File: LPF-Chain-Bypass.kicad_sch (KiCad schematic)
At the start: 2 parts, among them K9 HK19F-DCxxV-SHC, SW2 SW_SPDT

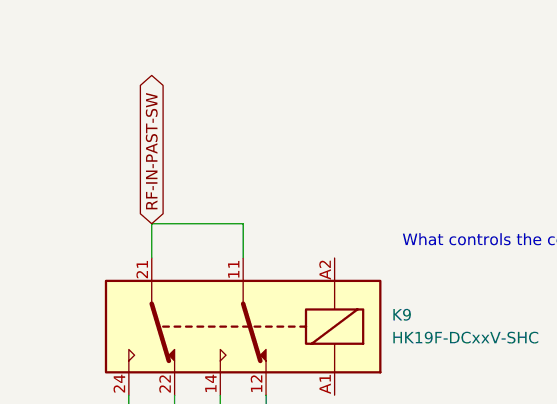
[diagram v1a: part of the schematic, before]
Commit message: RF-IN-PAST-SW now RF-INTO-FILTERS
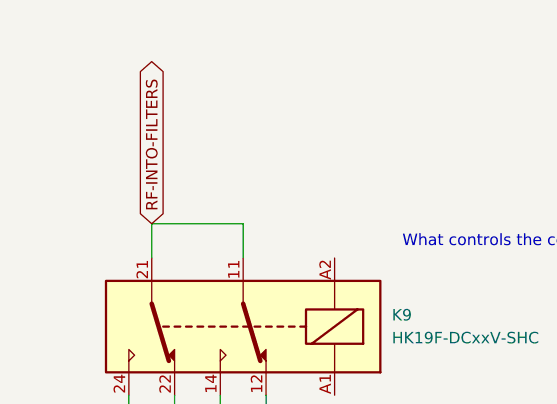
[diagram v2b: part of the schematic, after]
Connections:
- net RF-IN-PAST-SW renamed RF-INTO-FILTERS
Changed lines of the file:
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@@
 		)
 	)
-	(global_label "RF-IN-PAST-SW"
+	(global_label "RF-INTO-FILTERS"
 		(shape bidirectional)
 		(at 57.15 78.74 90)
@@
 		)
 		(property "Intersheetrefs" "${INTERSHEET_REFS}"
-			(at 57.15 58.436 90)
+			(at 57.15 57.5893 90)
 			(effects
 				(font

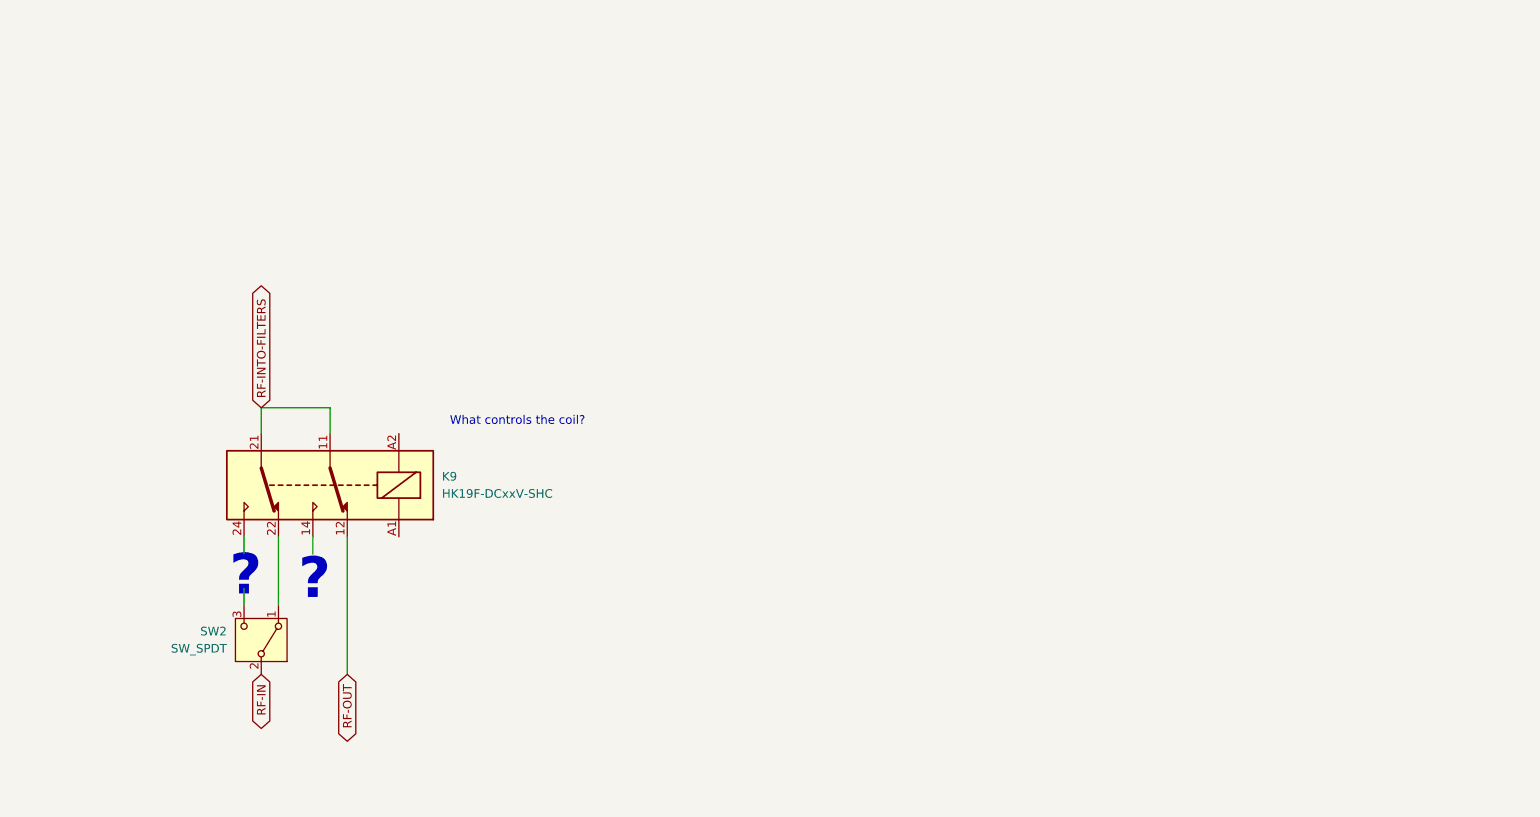
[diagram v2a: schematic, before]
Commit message: trying to get K1 & K2 appear in multiple places, yet be recognized as identical.  Currently reporting dup K1
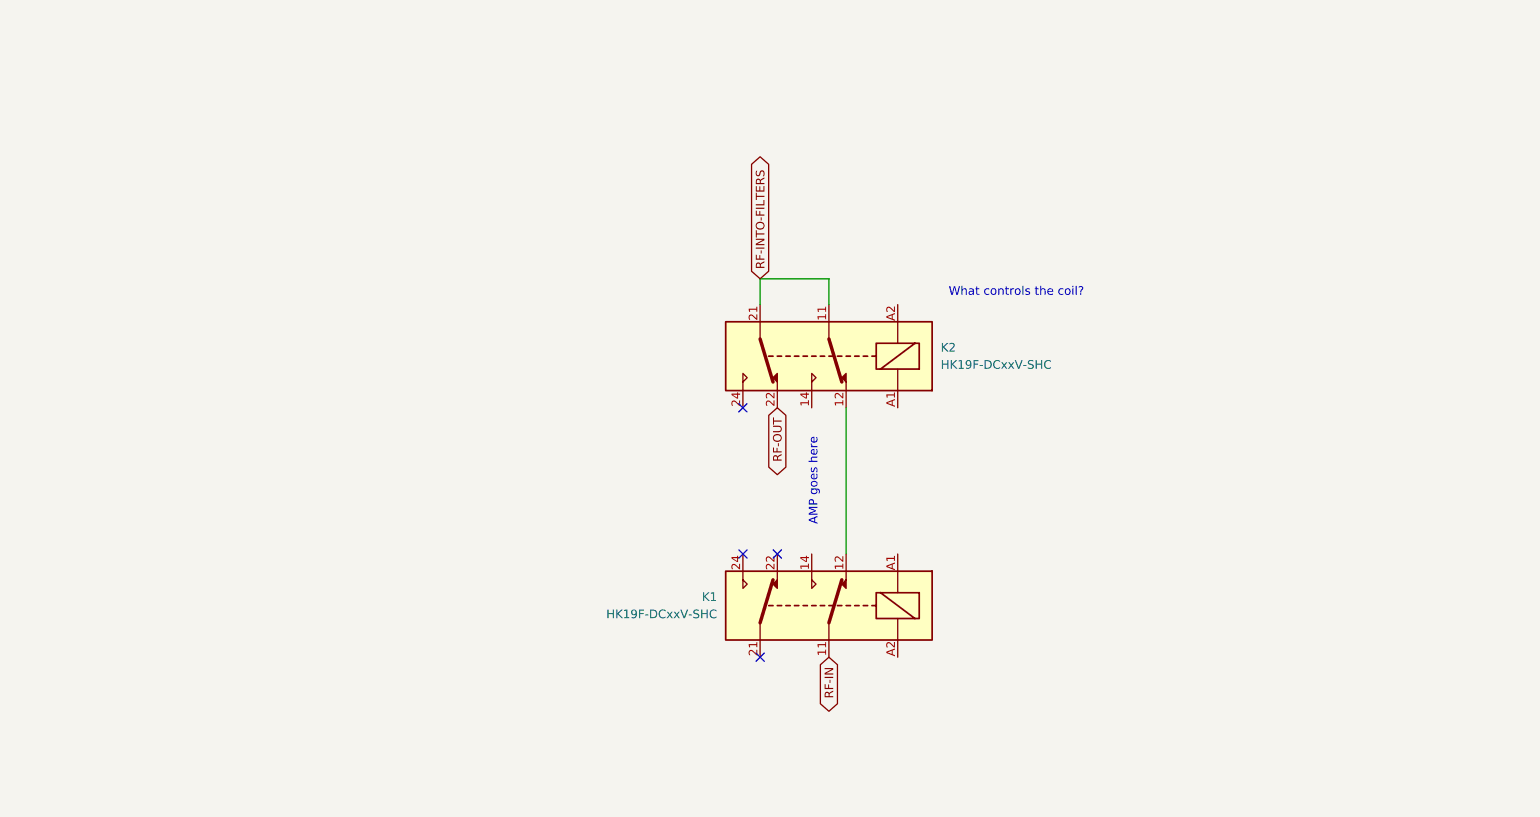
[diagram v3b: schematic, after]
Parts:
- removed SW2: SW_SPDT, symbol Switch:SW_SPDT
- added K1: HK19F-DCxxV-SHC, Relay_THT:Relay_DPDT_Finder_30.22, symbol Relay:HK19F-DCxxV-SHC
- renumbered K9 to K2
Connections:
- net RF-IN: now also K1.11
- net RF-OUT: now also K2.22; no longer K2.12
- new net: K1.12, K2.12
- no-connect marks 0 -> 4
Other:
- note added: "AMP goes here"
- note removed: "?"
- moved on the sheet: K2
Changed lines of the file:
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@@
 		(company "WA7GIL")
 	)
-	(wire
-		(pts
-			(xy 57.15 78.74) (xy 67.31 78.74)
-		)
-		(stroke
-			(width 0)
-			(type default)
-		)
-	)
-	(wire
-		(pts
-			(xy 69.85 97.79) (xy 69.85 118.11)
-		)
-		(stroke
-			(width 0)
-			(type default)
-		)
-	)
-	(wire
-		(pts
-			(xy 57.15 82.55) (xy 57.15 78.74)
-		)
-		(stroke
-			(width 0)
-			(type default)
-		)
-	)
-	(wire
-		(pts
-			(xy 64.77 97.79) (xy 64.77 100.33)
-		)
-		(stroke
-			(width 0)
-			(type default)
-		)
-	)
-	(wire
-		(pts
-			(xy 59.69 97.79) (xy 59.69 107.95)
-		)
-		(stroke
-			(width 0)
-			(type default)
-		)
-	)
-	(wire
-		(pts
-			(xy 54.61 100.33) (xy 54.61 97.79)
-		)
-		(stroke
-			(width 0)
-			(type default)
-		)
-	)
-	(wire
-		(pts
-			(xy 67.31 78.74) (xy 67.31 82.55)
-		)
-		(stroke
-			(width 0)
-			(type default)
-		)
-	)
-	(wire
-		(pts
-			(xy 54.61 105.41) (xy 54.61 107.95)
-		)
-		(stroke
-			(width 0)
-			(type default)
-		)
-	)
-	(text "?"
-		(exclude_from_sim no)
-		(at 54.864 103.632 0)
-		(effects
-			(font
-				(size 6 6)
-				(thickness 1.2)
-				(bold yes)
-			)
-		)
-	)
-	(text "?"
-		(exclude_from_sim no)
-		(at 65.024 104.14 0)
-		(effects
-			(font
-				(size 6 6)
-				(thickness 1.2)
-				(bold yes)
+	(no_connect
+		(at 128.27 100.33)
+	)
+	(no_connect
+		(at 130.81 115.57)
+	)
+	(no_connect
+		(at 133.35 100.33)
+	)
+	(no_connect
+		(at 128.27 78.74)
+	)
+	(wire
+		(pts
+			(xy 130.81 59.69) (xy 140.97 59.69)
+		)
+		(stroke
+			(width 0)
+			(type default)
+		)
+	)
+	(wire
+		(pts
+			(xy 143.51 78.74) (xy 143.51 100.33)
+		)
+		(stroke
+			(width 0)
+			(type default)
+		)
+	)
+	(wire
+		(pts
+			(xy 130.81 63.5) (xy 130.81 59.69)
+		)
+		(stroke
+			(width 0)
+			(type default)
+		)
+	)
+	(wire
+		(pts
+			(xy 140.97 59.69) (xy 140.97 63.5)
+		)
+		(stroke
+			(width 0)
+			(type default)
+		)
+	)
+	(text "AMP goes here"
+		(exclude_from_sim no)
+		(at 138.684 89.662 90)
+		(effects
+			(font
+				(size 1.27 1.27)
 			)
 		)
@@
 	(text "What controls the coil?"
 		(exclude_from_sim no)
-		(at 94.996 80.772 0)
+		(at 168.656 61.722 0)
 		(effects
 			(font
@@
 	(global_label "RF-OUT"
 		(shape bidirectional)
-		(at 69.85 118.11 270)
+		(at 133.35 78.74 270)
 		(fields_autoplaced yes)
 		(effects
@@
 		)
 		(property "Intersheetrefs" "${INTERSHEET_REFS}"
-			(at 69.85 129.7659 90)
+			(at 133.35 90.3959 90)
 			(effects
 				(font
@@
 	(global_label "RF-INTO-FILTERS"
 		(shape bidirectional)
-		(at 57.15 78.74 90)
+		(at 130.81 59.69 90)
 		(fields_autoplaced yes)
 		(effects
@@
 		)
 		(property "Intersheetrefs" "${INTERSHEET_REFS}"
-			(at 57.15 57.5893 90)
+			(at 130.81 38.5393 90)
 			(effects
 				(font
@@
 	(global_label "RF-IN"
 		(shape bidirectional)
-		(at 57.15 118.11 270)
+		(at 140.97 115.57 270)
 		(fields_autoplaced yes)
 		(effects
@@
 		)
 		(property "Intersheetrefs" "${INTERSHEET_REFS}"
-			(at 57.15 128.0726 90)
+			(at 140.97 125.5326 90)
 			(effects
 				(font
@@
 	)
 	(symbol
-		(lib_id "Switch:SW_SPDT")
-		(at 57.15 113.03 270)
-		(mirror x)
+		(lib_id "Relay:HK19F-DCxxV-SHC")
+		(at 140.97 71.12 180)
 		(unit 1)
 		(exclude_from_sim no)
@@
 		(on_board yes)
 		(dnp no)
-		(property "Reference" "SW2"
-			(at 52.07 111.7599 90)
-			(effects
-				(font
-					(size 1.27 1.27)
-				)
-				(justify right)
-			)
-		)
-		(property "Value" "SW_SPDT"
-			(at 52.07 114.2999 90)
-			(effects
-				(font
-					(size 1.27 1.27)
-				)
-				(justify right)
-			)
-		)
-		(property "Footprint" ""
-			(at 57.15 113.03 0)
-			(effects
-				(font
-					(size 1.27 1.27)
-				)
-				(hide yes)
-			)
-		)
-		(property "Datasheet" "~"
-			(at 49.53 113.03 0)
-			(effects
-				(font
-					(size 1.27 1.27)
-				)
-				(hide yes)
-			)
-		)
-		(property "Description" "Switch, single pole double throw"
-			(at 57.15 113.03 0)
-			(effects
-				(font
-					(size 1.27 1.27)
-				)
-				(hide yes)
-			)
-		)
-		(pin "3"
-		)
-		(pin "1"
-		)
-		(pin "2"
+		(fields_autoplaced yes)
+		(property "Reference" "K2"
+			(at 157.48 69.8499 0)
+			(effects
+				(font
+					(size 1.27 1.27)
+				)
+				(justify right)
+			)
+		)
+		(property "Value" "HK19F-DCxxV-SHC"
+			(at 157.48 72.3899 0)
+			(effects
+				(font
+					(size 1.27 1.27)
+				)
+				(justify right)
+			)
+		)
+		(property "Footprint" "Relay_THT:Relay_DPDT_Finder_30.22"
+			(at 158.75 58.42 0)
+			(effects
+				(font
+					(size 1.27 1.27)
+				)
+				(justify left)
+				(hide yes)
+			)
+		)
+		(property "Datasheet" "https://www.lcsc.com/datasheet/lcsc_datasheet_1810201512_Ningbo-Keke-New-Era-Appliance-HK19F-DC12V-SHG_C42803.pdf"
+			(at 140.97 53.34 0)
+			(effects
+				(font
+					(size 1.27 1.27)
+				)
+				(hide yes)
+			)
+		)
+		(property "Description" "HuiKe 19F monostable relay, DPDT, 1A"
+			(at 139.7 55.88 0)
+			(effects
+				(font
+					(size 1.27 1.27)
+				)
+				(hide yes)
+			)
+		)
+		(pin "11"
+		)
+		(pin "14"
+		)
+		(pin "21"
+		)
+		(pin "12"
+		)
+		(pin "22"
+		)
+		(pin "A2"
+		)
+		(pin "A1"
+		)
+		(pin "24"
 		)
 		(instances
 			(project ""
 				(path "/e63e39d7-6ac0-4ffd-8aa3-1841a4541b55/437da5b9-3c1b-43a3-b733-5d9a574d228b"
-					(reference "SW2")
+					(reference "K2")
 					(unit 1)
 				)
@@
 	(symbol
 		(lib_id "Relay:HK19F-DCxxV-SHC")
-		(at 67.31 90.17 180)
+		(at 140.97 107.95 0)
+		(mirror y)
 		(unit 1)
 		(exclude_from_sim no)
@@
 		(on_board yes)
 		(dnp no)
-		(fields_autoplaced yes)
-		(property "Reference" "K9"
-			(at 83.82 88.8999 0)
-			(effects
-				(font
-					(size 1.27 1.27)
-				)
-				(justify right)
+		(property "Reference" "K1"
+			(at 124.46 106.6799 0)
+			(effects
+				(font
+					(size 1.27 1.27)
+				)
+				(justify left)
 			)
 		)
 		(property "Value" "HK19F-DCxxV-SHC"
-			(at 83.82 91.4399 0)
-			(effects
-				(font
-					(size 1.27 1.27)
-				)
-				(justify right)
+			(at 124.46 109.2199 0)
+			(effects
+				(font
+					(size 1.27 1.27)
+				)
+				(justify left)
 			)
 		)
 		(property "Footprint" "Relay_THT:Relay_DPDT_Finder_30.22"
-			(at 85.09 77.47 0)
+			(at 158.75 120.65 0)
 			(effects
 				(font
@@
 		)
 		(property "Datasheet" "https://www.lcsc.com/datasheet/lcsc_datasheet_1810201512_Ningbo-Keke-New-Era-Appliance-HK19F-DC12V-SHG_C42803.pdf"
-			(at 67.31 72.39 0)
+			(at 140.97 125.73 0)
 			(effects
 				(font
@@
 		)
 		(property "Description" "HuiKe 19F monostable relay, DPDT, 1A"
-			(at 66.04 74.93 0)
-			(effects
-				(font
-					(size 1.27 1.27)
-				)
-				(hide yes)
-			)
+			(at 139.7 123.19 0)
+			(effects
+				(font
+					(size 1.27 1.27)
+				)
+				(hide yes)
+			)
+		)
+		(pin "A2"
+		)
+		(pin "A1"
+		)
+		(pin "22"
+		)
+		(pin "21"
+		)
+		(pin "24"
+		)
+		(pin "14"
+		)
+		(pin "12"
 		)
 		(pin "11"
 		)
-		(pin "14"
-		)
-		(pin "21"
-		)
-		(pin "12"
-		)
-		(pin "22"
-		)
-		(pin "A2"
-		)
-		(pin "A1"
-		)
-		(pin "24"
-		)
 		(instances
-			(project ""
+			(project "QMX-amp"
 				(path "/e63e39d7-6ac0-4ffd-8aa3-1841a4541b55/437da5b9-3c1b-43a3-b733-5d9a574d228b"
-					(reference "K9")
+					(reference "K1")
 					(unit 1)
 				)

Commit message: checkpoint progress from 240810
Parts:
- added C99: C_Polarized, symbol Device:C_Polarized
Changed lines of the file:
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@@
+		)
+	)
+	(symbol
+		(lib_id "Device:C_Polarized")
+		(at 209.55 133.35 0)
+		(unit 1)
+		(exclude_from_sim no)
+		(in_bom yes)
+		(on_board yes)
+		(dnp no)
+		(fields_autoplaced yes)
+		(property "Reference" "C99"
+			(at 213.36 131.1909 0)
+			(effects
+				(font
+					(size 1.27 1.27)
+				)
+				(justify left)
+			)
+		)
+		(property "Value" "C_Polarized"
+			(at 213.36 133.7309 0)
+			(effects
+				(font
+					(size 1.27 1.27)
+				)
+				(justify left)
+			)
+		)
+		(property "Footprint" ""
+			(at 210.5152 137.16 0)
+			(effects
+				(font
+					(size 1.27 1.27)
+				)
+				(hide yes)
+			)
+		)
+		(property "Datasheet" "~"
+			(at 209.55 133.35 0)
+			(effects
+				(font
+					(size 1.27 1.27)
+				)
+				(hide yes)
+			)
+		)
+		(property "Description" "Polarized capacitor"
+			(at 209.55 133.35 0)
+			(effects
+				(font
+					(size 1.27 1.27)
+				)
+				(hide yes)
+			)
+		)
+		(pin "2"
+		)
+		(pin "1"
+		)
+		(instances
+			(project "QMX-amp"
+				(path "/e63e39d7-6ac0-4ffd-8aa3-1841a4541b55/437da5b9-3c1b-43a3-b733-5d9a574d228b"
+					(reference "C99")
+					(unit 1)
+				)
+			)
 		)
 	)

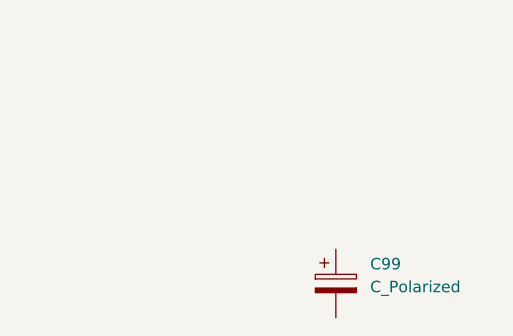
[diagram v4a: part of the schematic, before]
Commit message: changed +5V and +12V from global symbol to the more normal voltage busses
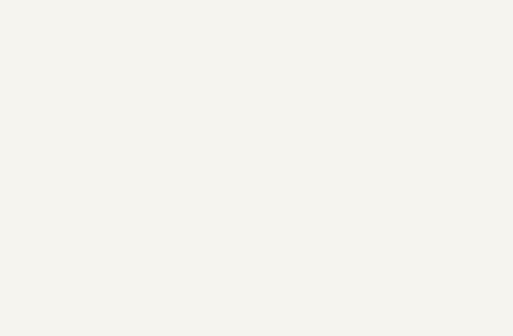
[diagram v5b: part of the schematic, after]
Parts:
- removed C99: C_Polarized, symbol Device:C_Polarized
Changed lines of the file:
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@@
-		)
-	)
-	(symbol
-		(lib_id "Device:C_Polarized")
-		(at 209.55 133.35 0)
-		(unit 1)
-		(exclude_from_sim no)
-		(in_bom yes)
-		(on_board yes)
-		(dnp no)
-		(fields_autoplaced yes)
-		(property "Reference" "C99"
-			(at 213.36 131.1909 0)
-			(effects
-				(font
-					(size 1.27 1.27)
-				)
-				(justify left)
-			)
-		)
-		(property "Value" "C_Polarized"
-			(at 213.36 133.7309 0)
-			(effects
-				(font
-					(size 1.27 1.27)
-				)
-				(justify left)
-			)
-		)
-		(property "Footprint" ""
-			(at 210.5152 137.16 0)
-			(effects
-				(font
-					(size 1.27 1.27)
-				)
-				(hide yes)
-			)
-		)
-		(property "Datasheet" "~"
-			(at 209.55 133.35 0)
-			(effects
-				(font
-					(size 1.27 1.27)
-				)
-				(hide yes)
-			)
-		)
-		(property "Description" "Polarized capacitor"
-			(at 209.55 133.35 0)
-			(effects
-				(font
-					(size 1.27 1.27)
-				)
-				(hide yes)
-			)
-		)
-		(pin "2"
-		)
-		(pin "1"
-		)
-		(instances
-			(project "QMX-amp"
-				(path "/e63e39d7-6ac0-4ffd-8aa3-1841a4541b55/437da5b9-3c1b-43a3-b733-5d9a574d228b"
-					(reference "C99")
-					(unit 1)
-				)
-			)
 		)
 	)

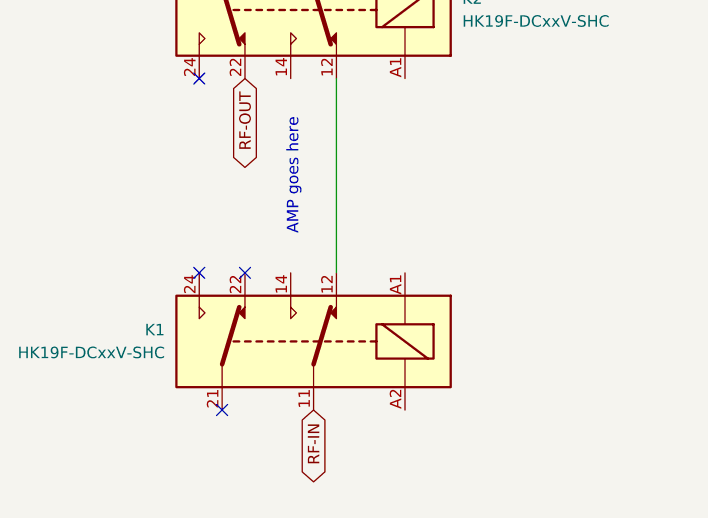
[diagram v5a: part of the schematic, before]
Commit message: could not figure out how to have two instances of K1 so I used global labels.  STINKY HACK
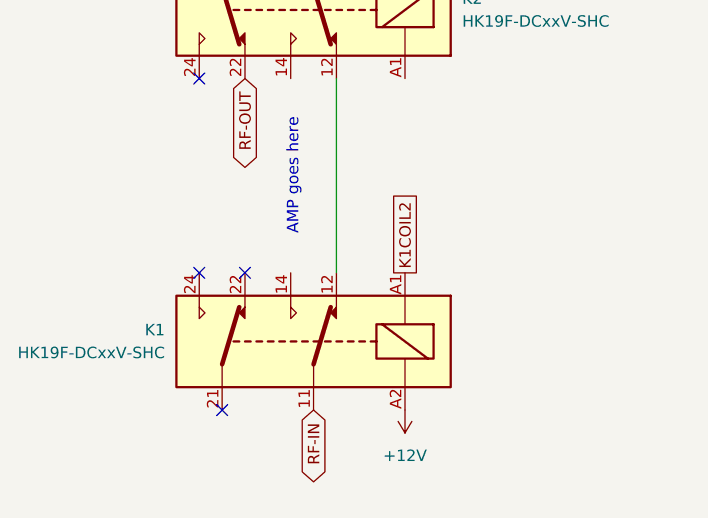
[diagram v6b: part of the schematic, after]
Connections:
- net K1COIL2: now reaches K1.A1
- net +12V: now reaches K1.A2
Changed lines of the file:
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@@
+		)
+	)
+	(global_label "K1COIL2"
+		(shape passive)
+		(at 151.13 100.33 90)
+		(fields_autoplaced yes)
+		(effects
+			(font
+				(size 1.27 1.27)
+			)
+			(justify left)
+		)
+		(property "Intersheetrefs" "${INTERSHEET_REFS}"
+			(at 151.13 90.3433 90)
+			(effects
+				(font
+					(size 1.27 1.27)
+				)
+				(justify left)
+				(hide yes)
+			)
+		)
+	)
+	(symbol
+		(lib_id "power:+12V")
+		(at 151.13 115.57 180)
+		(unit 1)
+		(exclude_from_sim no)
+		(in_bom yes)
+		(on_board yes)
+		(dnp no)
+		(fields_autoplaced yes)
+		(property "Reference" "#PWR033"
+			(at 151.13 111.76 0)
+			(effects
+				(font
+					(size 1.27 1.27)
+				)
+				(hide yes)
+			)
+		)
+		(property "Value" "+12V"
+			(at 151.13 120.65 0)
+			(effects
+				(font
+					(size 1.27 1.27)
+				)
+			)
+		)
+		(property "Footprint" ""
+			(at 151.13 115.57 0)
+			(effects
+				(font
+					(size 1.27 1.27)
+				)
+				(hide yes)
+			)
+		)
+		(property "Datasheet" ""
+			(at 151.13 115.57 0)
+			(effects
+				(font
+					(size 1.27 1.27)
+				)
+				(hide yes)
+			)
+		)
+		(property "Description" "Power symbol creates a global label with name \"+12V\""
+			(at 151.13 115.57 0)
+			(effects
+				(font
+					(size 1.27 1.27)
+				)
+				(hide yes)
+			)
+		)
+		(pin "1"
+		)
+		(instances
+			(project ""
+				(path "/e63e39d7-6ac0-4ffd-8aa3-1841a4541b55/437da5b9-3c1b-43a3-b733-5d9a574d228b"
+					(reference "#PWR033")
+					(unit 1)
+				)
+			)
 		)
 	)
